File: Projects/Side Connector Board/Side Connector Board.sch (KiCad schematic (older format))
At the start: 22 parts, among them J1 Conn_02x05_Top_Bottom, J10 Conn_02x05_Top_Bottom, J11 Conn_02x05_Top_Bottom, J12 Conn_02x05_Top_Bottom, J13 Conn_02x04_Top_Bottom, J14 Conn_02x04_Top_Bottom, J15 Conn_02x04_Top_Bottom, J16 Conn_02x04_Top_Bottom, J2 Conn_02x05_Top_Bottom, J3 Conn_02x05_Top_Bottom, J4 Conn_02x05_Top_Bottom, J5 Conn_02x05_Top_Bottom, J6 Conn_02x05_Top_Bottom, J7 Conn_02x05_Top_Bottom, J8 Conn_02x05_Top_Bottom, J9 Conn_02x05_Top_Bottom, U1 PowerConnector, U2 PowerConnector, U3 PowerConnector, U4 PowerConnector, U5 PowerConnector, U6 PowerConnector

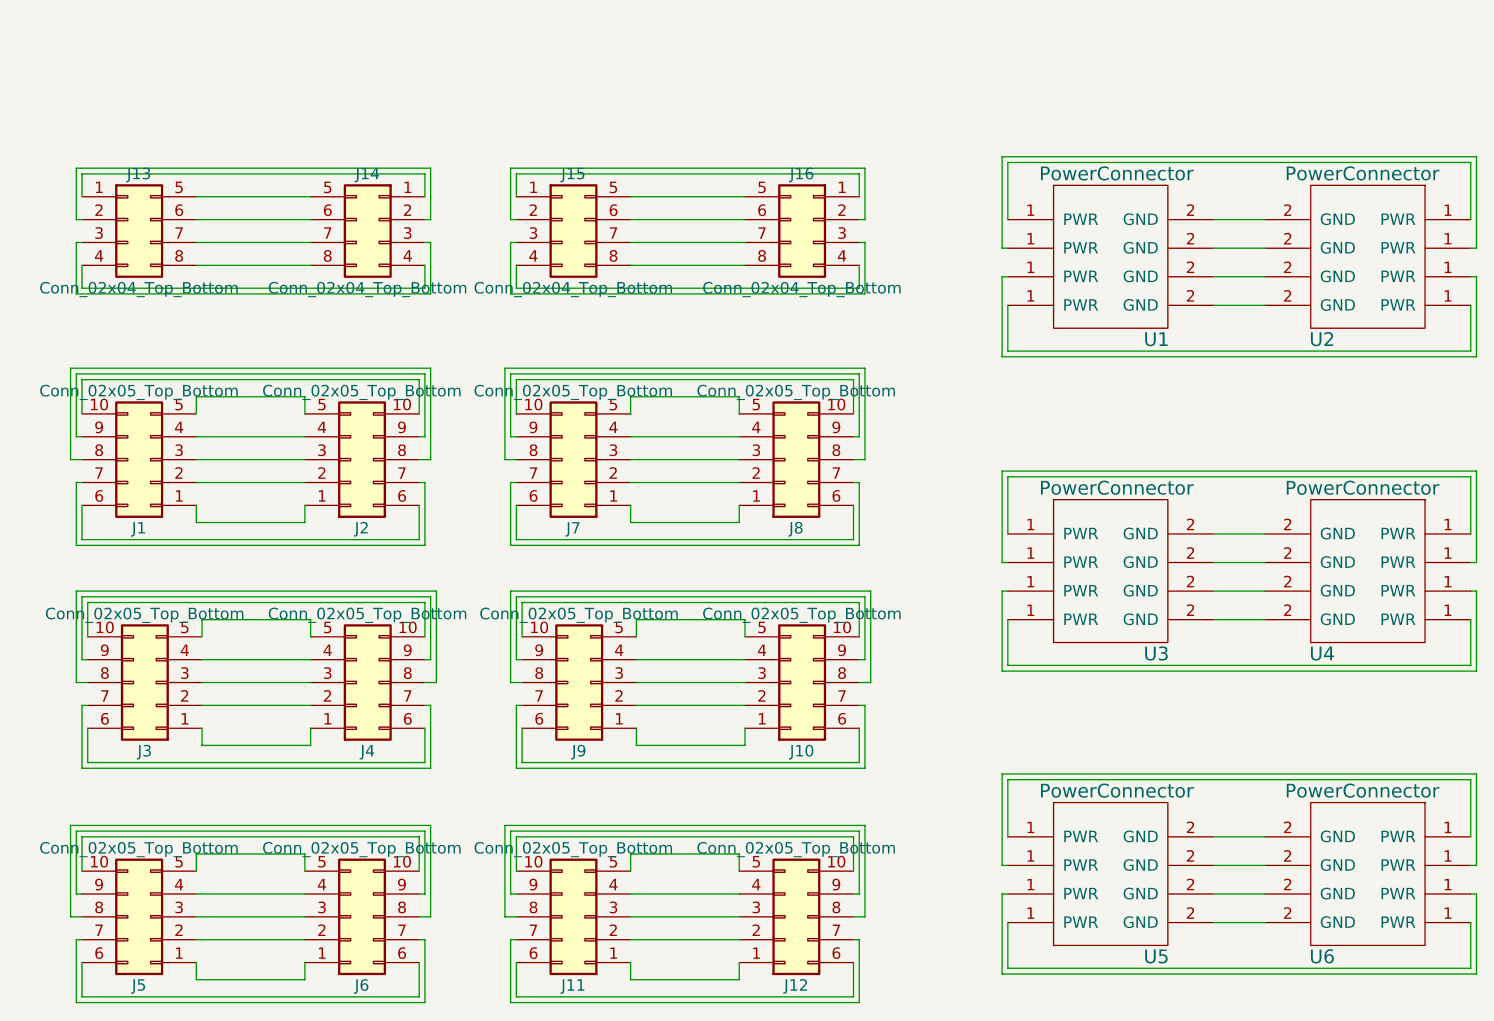
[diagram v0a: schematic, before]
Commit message: Edited & re-associated schematic. Replaced 10 pin Molex connector with 8 pin
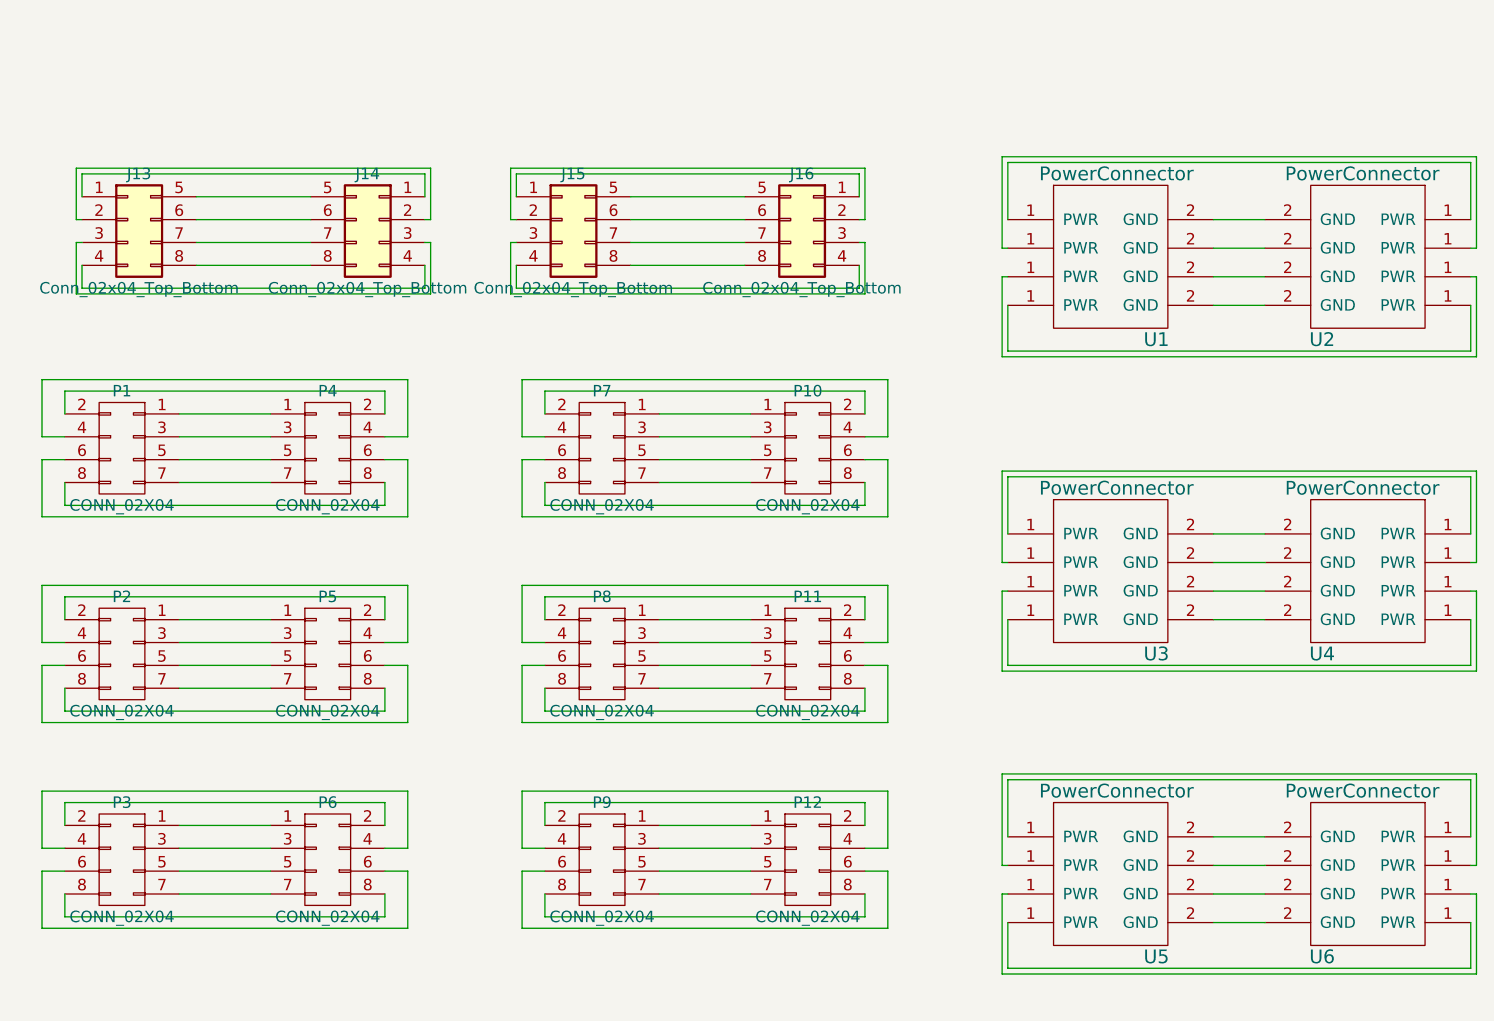
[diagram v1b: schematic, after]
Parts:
- removed J1, J10, J11, J12, J2, J3, J4, J5, J6, J7, J8, J9: Conn_02x05_Top_Bottom, Connectors_Molex:Molex_MiniFit-JR-5569-10A2_2x05x4.20mm_Angled, symbol Conn_02x05_Top_Bottom
- added P1, P10, P11, P12, P2, P3, P4, P5, P6, P7, P8, P9: CONN_02X04, USST-footprints:Molex_MiniFit-JR-5569-08A2_2x04x4.20mm_Angled_Overhang, symbol CONN_02X04
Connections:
- new net: U1.1 (PWR), U2.1 (PWR) (x3)
- new net: U1.2 (GND), U2.2 (GND) (x3)
- new net: U3.1 (PWR), U4.1 (PWR) (x3)
- new net: U3.2 (GND), U4.2 (GND) (x3)
- new net: U5.1 (PWR), U6.1 (PWR) (x3)
- new net: U5.2 (GND), U6.2 (GND) (x3)
- new net: P11.1 (P1), P8.1 (P1)
- new net: P11.2 (P2), P8.2 (P2)
- new net: P11.3 (P3), P8.3 (P3)
- new net: P11.4 (P4), P8.4 (P4)
- new net: P11.5 (P5), P8.5 (P5)
- new net: P11.6 (P6), P8.6 (P6)
- new net: P11.7 (P7), P8.7 (P7)
- new net: P11.8 (P8), P8.8 (P8)
- new net: P10.1 (P1), P7.1 (P1)
- new net: P10.2 (P2), P7.2 (P2)
- new net: P10.3 (P3), P7.3 (P3)
- new net: P10.4 (P4), P7.4 (P4)
- new net: P10.5 (P5), P7.5 (P5)
- new net: P10.6 (P6), P7.6 (P6)
- new net: P10.7 (P7), P7.7 (P7)
- new net: P10.8 (P8), P7.8 (P8)
- new net: P2.1 (P1), P5.1 (P1)
- new net: P2.2 (P2), P5.2 (P2)
- new net: P2.3 (P3), P5.3 (P3)
- new net: P2.4 (P4), P5.4 (P4)
- new net: P2.5 (P5), P5.5 (P5)
- new net: P2.6 (P6), P5.6 (P6)
- new net: P2.7 (P7), P5.7 (P7)
- new net: P2.8 (P8), P5.8 (P8)
- new net: P1.1 (P1), P4.1 (P1)
- new net: P1.2 (P2), P4.2 (P2)
- new net: P1.3 (P3), P4.3 (P3)
- new net: P1.4 (P4), P4.4 (P4)
- new net: P1.5 (P5), P4.5 (P5)
- new net: P1.6 (P6), P4.6 (P6)
- new net: P1.7 (P7), P4.7 (P7)
- new net: P1.8 (P8), P4.8 (P8)
- new net: P12.1 (P1), P9.1 (P1)
- new net: P12.2 (P2), P9.2 (P2)
- new net: P12.3 (P3), P9.3 (P3)
- new net: P12.4 (P4), P9.4 (P4)
- new net: P12.5 (P5), P9.5 (P5)
- new net: P12.6 (P6), P9.6 (P6)
- new net: P12.7 (P7), P9.7 (P7)
- new net: P12.8 (P8), P9.8 (P8)
- new net: P3.1 (P1), P6.1 (P1)
- new net: P3.2 (P2), P6.2 (P2)
- new net: P3.3 (P3), P6.3 (P3)
- new net: P3.4 (P4), P6.4 (P4)
- new net: P3.5 (P5), P6.5 (P5)
- new net: P3.6 (P6), P6.6 (P6)
- new net: P3.7 (P7), P6.7 (P7)
- new net: P3.8 (P8), P6.8 (P8)

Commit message: Added USB3 to schematic. Finished GERBER Files
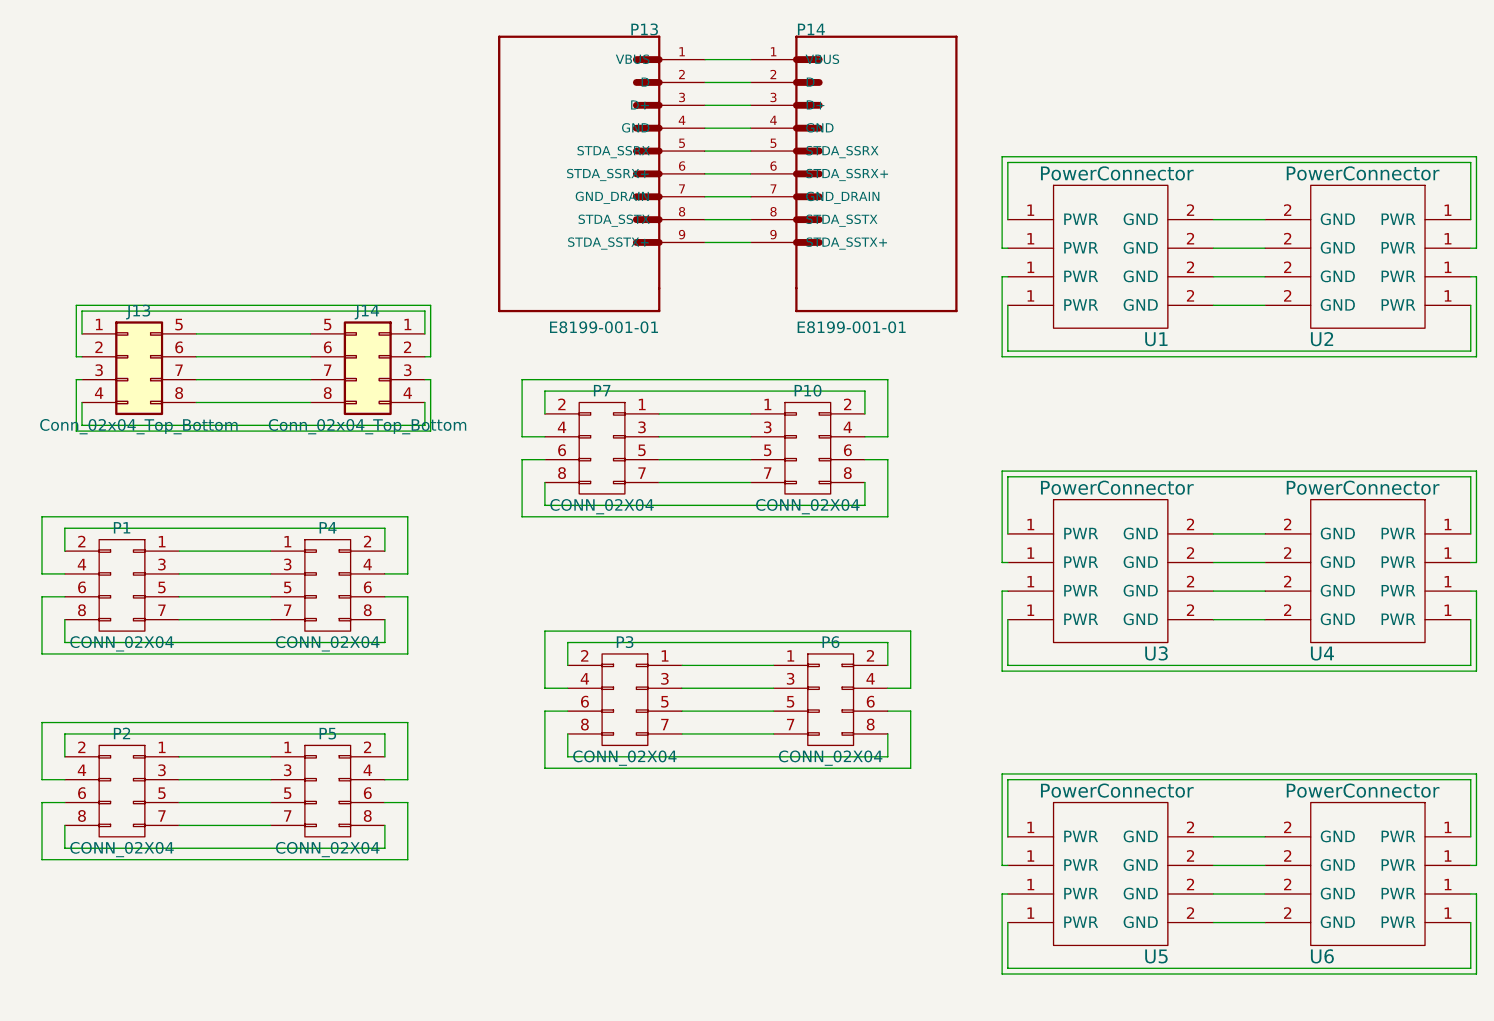
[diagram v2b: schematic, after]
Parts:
- removed J15, J16: Conn_02x04_Top_Bottom, USST-footprints:USB_A_Stacked_AE11131-ND, symbol Conn_02x04_Top_Bottom
- removed P11, P12, P8, P9: CONN_02X04, USST-footprints:Molex_MiniFit-JR-5569-08A2_2x04x4.20mm_Angled_Overhang, symbol CONN_02X04
- added P13, P14: E8199-001-01, USST-footprints:USB3.0-A-3.0-TH-RA, symbol E8199-001-01
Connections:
- new net: U1.1 (PWR), U2.1 (PWR) (x3)
- new net: U1.2 (GND), U2.2 (GND) (x3)
- new net: U3.1 (PWR), U4.1 (PWR) (x3)
- new net: U3.2 (GND), U4.2 (GND) (x3)
- new net: U5.1 (PWR), U6.1 (PWR) (x3)
- new net: U5.2 (GND), U6.2 (GND) (x3)
- new net: P13.1 (VBUS), P14.1 (VBUS)
- new net: P13.2 (D), P14.2 (D)
- new net: P13.3 (D+), P14.3 (D+)
- new net: P13.4 (GND), P14.4 (GND)
- new net: P13.5 (STDA_SSRX), P14.5 (STDA_SSRX)
- new net: P13.6 (STDA_SSRX+), P14.6 (STDA_SSRX+)
- new net: P13.7 (GND_DRAIN), P14.7 (GND_DRAIN)
- new net: P13.8 (STDA_SSTX), P14.8 (STDA_SSTX)
- new net: P13.9 (STDA_SSTX+), P14.9 (STDA_SSTX+)
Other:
- moved on the sheet: J13, J14, P1, P2, P3, P4, P5, P6
